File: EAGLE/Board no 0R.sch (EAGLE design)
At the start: 168 parts, among them J1 JUMPER_SOLDER_1X2, J10 JUMPER_SOLDER_1X2, J11 JUMPER_SOLDER_1X2, J12 KF301-2P, J2 JUMPER_SOLDER_1X2, J3 JUMPER_SOLDER_1X2, J4 JUMPER_SOLDER_1X2, J5 JUMPER_SOLDER_1X2, J6 JUMPER_SOLDER_1X2, J8 KF301-2P, J9 JUMPER_SOLDER_1X2, Q1 500mA/300V, Q2 500mA/300V, Q3 FDN337N, U1 SN74HC04PW, U2 ESP32-WROOM-32, U3 CH340C, U4 AMS1117, U6 PCA9635PW, U7 SN74HC04PW, U8 SN74HC04PW, U9 LTC1694IS5#TRPBF, X1 JST-XH-04-PIN-LONG-PAD, X2 JST-XH-04-PIN-LONG-PAD, X3 JST-XH-02-PIN-LONG-PAD

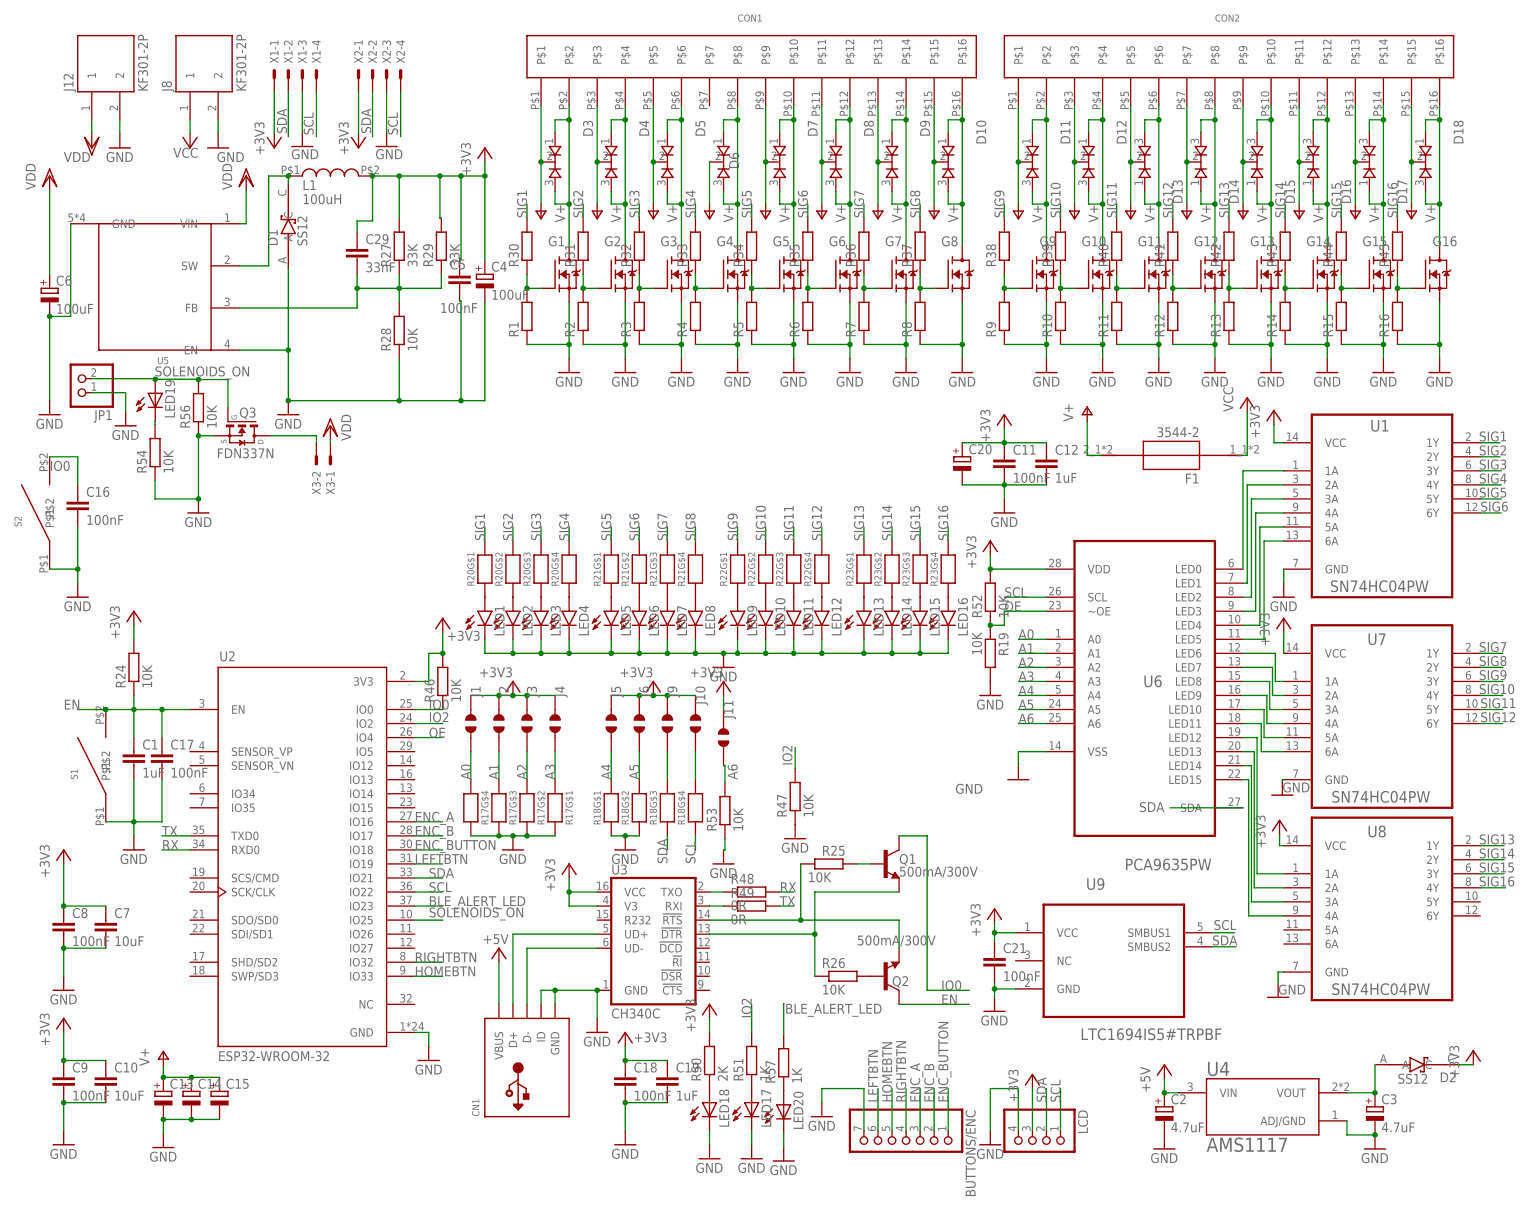
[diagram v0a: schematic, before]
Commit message: Update EAGLE files to latest version
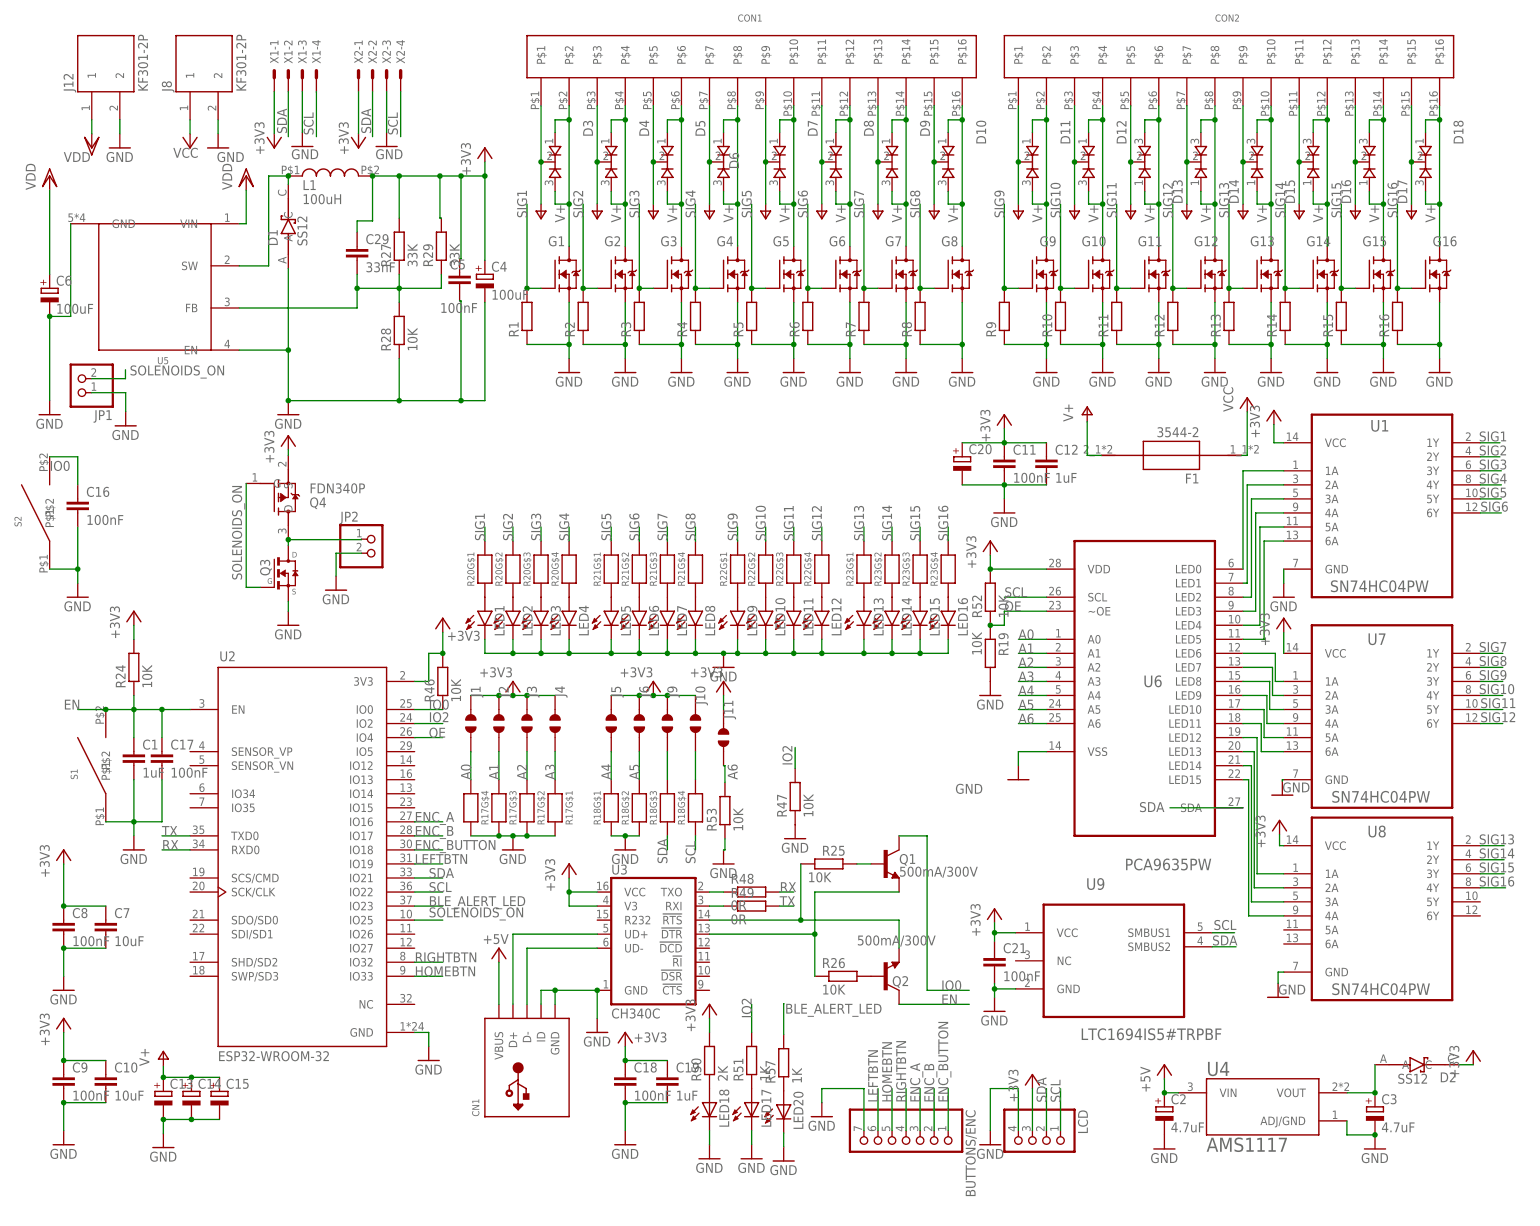
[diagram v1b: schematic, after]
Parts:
- removed LED19: (no value), dp_devices:LED-0603
- removed R30, R31, R32, R33, R34, R35, R36, R37, R38, R39, R40, R41, R42, R43, R44, R45: (no value), rcl:R-EU_R0603
- removed R54, R56: 10K, rcl:R-EU_R0603
- removed X3: JST-XH-02-PIN-LONG-PAD, Rembrandt Electronics - JST XH Connectors v1-0:JST-XH-02-PIN-LONG-PAD
- added JP2: (no value), pinhead:PINHD-1X2
- added Q4: FDN340P, FDN340P:FDN340P
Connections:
- removed net N$26: G1.G, R1.2, R30.1
- removed net N$45: G2.G, R2.2, R31.1
- removed net N$47: G3.G, R3.2, R32.1
- removed net N$49: G4.G, R33.1, R4.2
- removed net N$51: G5.G, R34.1, R5.2
- removed net N$52: G6.G, R35.1, R6.2
- removed net N$53: G7.G, R36.1, R7.2
- removed net N$55: G8.G, R37.1, R8.2
- removed net N$56: G9.G, R38.1, R9.2
- removed net N$57: G10.G, R10.2, R39.1
- removed net N$58: G11.G, R11.2, R40.1
- removed net N$59: G12.G, R12.2, R41.1
- removed net N$60: G13.G, R13.2, R42.1
- removed net N$61: G14.G, R14.2, R43.1
- removed net N$62: G15.G, R15.2, R44.1
- removed net N$63: G16.G, R16.2, R45.1
- removed net N$83: LED19.C, R54.2
- net +3V3: now also Q4.S
- net GND: now also JP2.2; no longer R54.1, R56.1
- net N$37: now also JP2.1, Q4.D; no longer X3-2.S
- net SIG1: now also G1.G, R1.2; no longer R30.2
- net SIG10: now also G10.G, R10.2; no longer R39.2
- net SIG11: now also G11.G, R11.2; no longer R40.2
- net SIG12: now also G12.G, R12.2; no longer R41.2
- net SIG13: now also G13.G, R13.2; no longer R42.2
- net SIG14: now also G14.G, R14.2; no longer R43.2
- net SIG15: now also G15.G, R15.2; no longer R44.2
- net SIG16: now also G16.G, R16.2; no longer R45.2
- net SIG2: now also G2.G, R2.2; no longer R31.2
- net SIG3: now also G3.G, R3.2; no longer R32.2
- net SIG4: now also G4.G, R4.2; no longer R33.2
- net SIG5: now also G5.G, R5.2; no longer R34.2
- net SIG6: now also G6.G, R6.2; no longer R35.2
- net SIG7: now also G7.G, R7.2; no longer R36.2
- net SIG8: now also G8.G, R8.2; no longer R37.2
- net SIG9: now also G9.G, R9.2; no longer R38.2
- net SOLENOIDS_ON: now also Q4.G; no longer LED19.A, R56.2
- net V+: now also CON1.P$7
- net VDD: no longer X3-1.S
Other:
- moved on the sheet: Q3
